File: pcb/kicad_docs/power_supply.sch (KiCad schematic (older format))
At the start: 22 parts, among them J10 ps_dc_htr_in_pcb, J7 ps_hv_dc_out_pcb, J8 ps_dc_htr_out_pcb, J9 ps_hv_ac_in_pcb

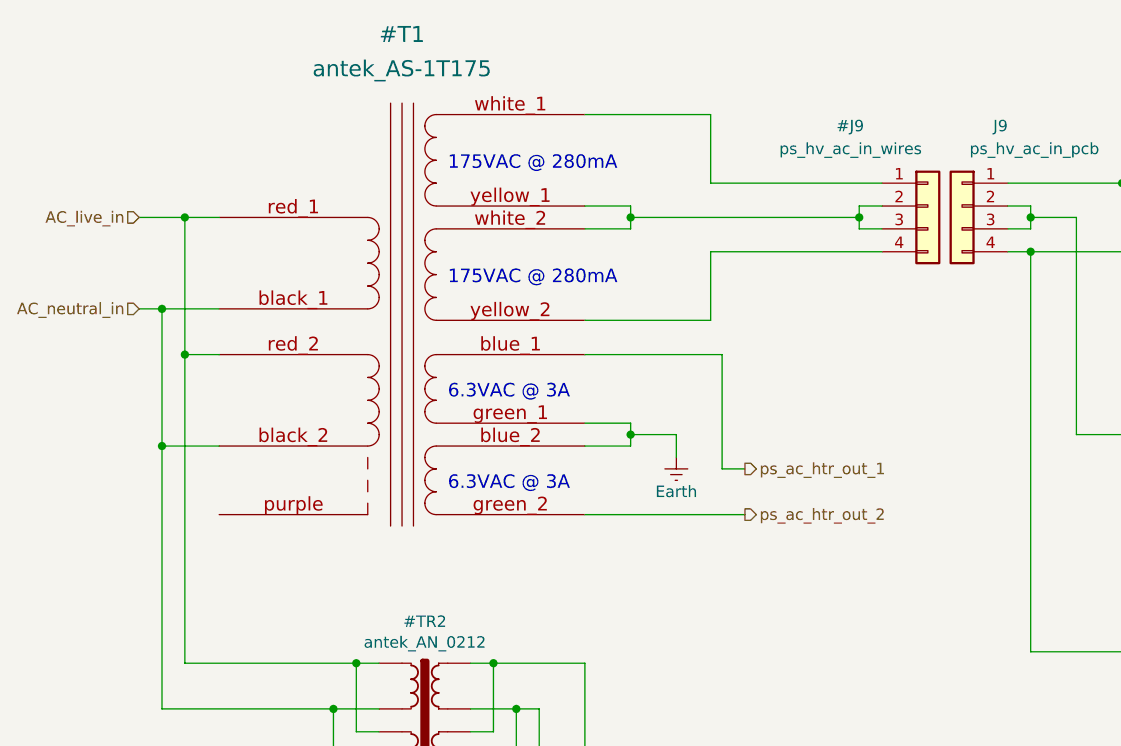
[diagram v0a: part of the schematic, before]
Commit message: add screen wire to power xformer
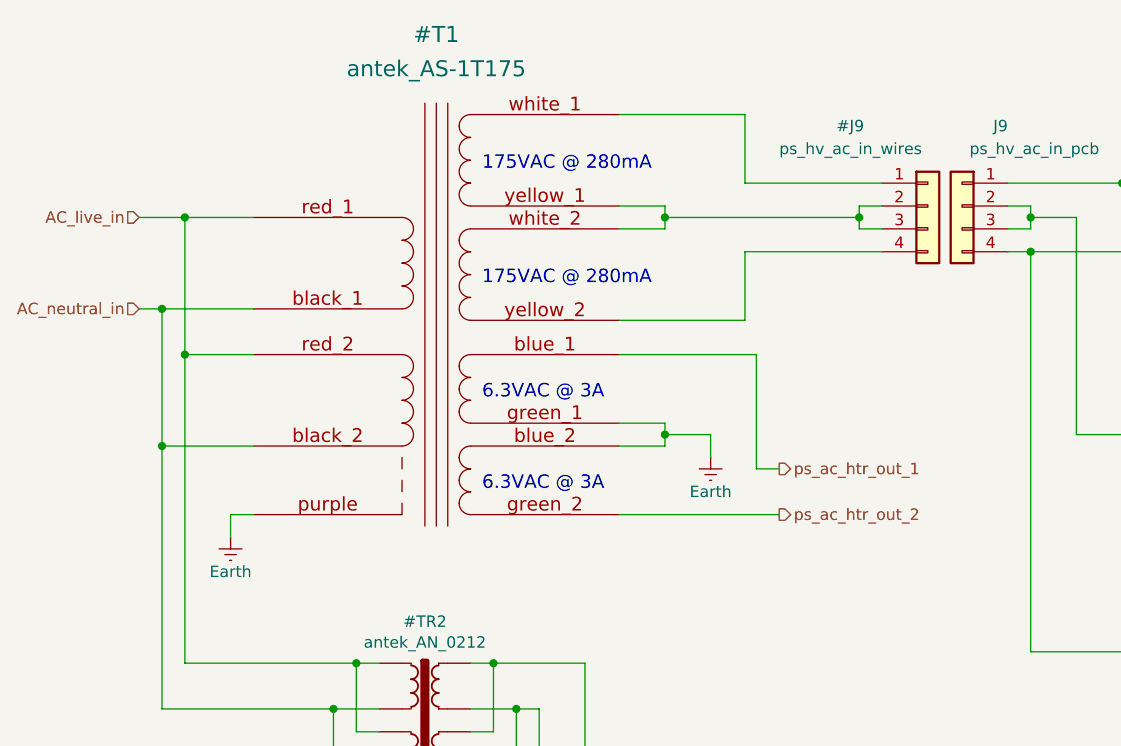
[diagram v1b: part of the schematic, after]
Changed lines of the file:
@@
 Sheet 4 4
 Title "It is the Champion"
-Date "2021-12-12"
+Date "2021-12-21"
 Rev "0.1"
 Comp ""
@@
 Text HLabel 1150 1750 0    50   Input ~ 0
 AC_live_in
-Text Notes 2500 2550 0    59   ~ 0
+Text Notes 2650 2550 0    59   ~ 0
 6.3VAC @ 3A
 Wire Wire Line
@@
 L custom_parts:antek_AS-1Txxx #T1
 U 1 1 61280AD8
-P 2300 2400
-F 0 "#T1" H 2300 3850 70  0000 C CNN
-F 1 "antek_AS-1T175" H 2300 3700 70  0000 C CNN
-F 2 "" H 2275 2475 60  0001 C CNN
-F 3 "" H 2275 2475 60  0000 C CNN
-	1    2300 2400
-	1    0    0    -1
-$EndComp
-Wire Wire Line
-	1500 2350 1350 2350
+P 2450 2400
+F 0 "#T1" H 2450 3850 70  0000 C CNN
+F 1 "antek_AS-1T175" H 2450 3700 70  0000 C CNN
+F 2 "" H 2425 2475 60  0001 C CNN
+F 3 "" H 2425 2475 60  0000 C CNN
+	1    2450 2400
+	1    0    0    -1
+$EndComp
+Wire Wire Line
+	1650 2350 1350 2350
 Wire Wire Line
 	1350 2350 1350 1750
 Wire Wire Line
-	1350 1750 1500 1750
-Wire Wire Line
-	1500 2750 1250 2750
+	1350 1750 1650 1750
+Wire Wire Line
+	1650 2750 1250 2750
 Wire Wire Line
 	1250 2750 1250 2150
 Wire Wire Line
-	1250 2150 1500 2150
+	1250 2150 1650 2150
 Connection ~ 1350 1750
 Connection ~ 1250 2150
 Wire Wire Line
-	3100 2650 3300 2650
+	3250 2650 3450 2650
 $Comp
 L Device:CP1 C17
@@
 Wire Wire Line
 	3650 5750 3650 5850
-Text Notes 2500 2950 0    59   ~ 0
+Text Notes 2650 2950 0    59   ~ 0
 6.3VAC @ 3A
 Wire Wire Line
-	3300 2750 3100 2750
+	3450 2750 3250 2750
 Wire Wire Line
 	3650 5150 3650 5050
@@
 $EndComp
 Wire Wire Line
-	3300 2750 3300 2700
-Wire Wire Line
-	3100 1800 3300 1800
-Wire Wire Line
-	3300 1800 3300 1750
-Wire Wire Line
-	3300 1700 3100 1700
-Text Notes 2500 1550 0    59   ~ 0
+	3450 2750 3450 2700
+Wire Wire Line
+	3250 1800 3450 1800
+Wire Wire Line
+	3450 1800 3450 1750
+Wire Wire Line
+	3450 1700 3250 1700
+Text Notes 2650 1550 0    59   ~ 0
 175VAC @ 280mA
 $Comp
@@
 L power:Earth #PWR?
 U 1 1 61F4E050
-P 3500 2800
+P 3650 2800
 AR Path="/61F4E050" Ref="#PWR?"  Part="1"
 AR Path="/61116F52/61F4E050" Ref="#PWR0103"  Part="1"
-F 0 "#PWR0103" H 3500 2550 50  0001 C CNN
-F 1 "Earth" H 3500 2650 50  0000 C CNN
-F 2 "" H 3500 2800 50  0001 C CNN
-F 3 "~" H 3500 2800 50  0001 C CNN
-	1    3500 2800
-	1    0    0    -1
-$EndComp
-Wire Wire Line
-	3500 2800 3500 2700
-Wire Wire Line
-	3500 2700 3300 2700
-Connection ~ 3300 2700
-Wire Wire Line
-	3300 2700 3300 2650
-Wire Wire Line
-	3800 2850 3700 2850
-Wire Wire Line
-	3700 2850 3700 2350
-Wire Wire Line
-	3100 2350 3700 2350
+F 0 "#PWR0103" H 3650 2550 50  0001 C CNN
+F 1 "Earth" H 3650 2650 50  0000 C CNN
+F 2 "" H 3650 2800 50  0001 C CNN
+F 3 "~" H 3650 2800 50  0001 C CNN
+	1    3650 2800
+	1    0    0    -1
+$EndComp
+Wire Wire Line
+	3650 2800 3650 2700
+Wire Wire Line
+	3650 2700 3450 2700
+Connection ~ 3450 2700
+Wire Wire Line
+	3450 2700 3450 2650
+Wire Wire Line
+	3950 2850 3850 2850
+Wire Wire Line
+	3850 2850 3850 2350
+Wire Wire Line
+	3250 2350 3850 2350
 Wire Wire Line
 	4300 1700 4300 1750
@@
 	4300 1700 4400 1700
 Wire Wire Line
-	4300 1750 3300 1750
+	4300 1750 3450 1750
 Connection ~ 4300 1750
 Wire Wire Line
 	4300 1750 4300 1800
 Wire Wire Line
-	4400 1600 3650 1600
-Wire Wire Line
-	3650 1600 3650 1300
-Wire Wire Line
-	3650 1300 3100 1300
-Wire Wire Line
-	3100 2200 3650 2200
-Wire Wire Line
-	3650 2200 3650 1900
-Wire Wire Line
-	3650 1900 4400 1900
+	4400 1600 3800 1600
+Wire Wire Line
+	3800 1600 3800 1300
+Wire Wire Line
+	3800 1300 3250 1300
+Wire Wire Line
+	3250 2200 3800 2200
+Wire Wire Line
+	3800 2200 3800 1900
+Wire Wire Line
+	3800 1900 4400 1900
 $Comp
 L Diode:1N4007 D4
@@
 Wire Wire Line
 	6050 1600 6150 1600
-Connection ~ 3300 1750
-Wire Wire Line
-	3300 1750 3300 1700
+Connection ~ 3450 1750
+Wire Wire Line
+	3450 1750 3450 1700
 Wire Wire Line
 	6950 3650 7250 3650
@@
 Wire Wire Line
 	5050 1750 5050 1800
-Text Notes 2500 2050 0    59   ~ 0
+Text Notes 2650 2050 0    59   ~ 0
 175VAC @ 280mA
 $Comp
@@
 	4800 6650 5400 6650
 Wire Wire Line
-	3100 3050 3800 3050
+	3250 3050 3950 3050
 Text Notes 3400 7050 0    50   ~ 0
 DC heater supply is referenced\nto the chassis through one of\nthe metal standoffs.
@@
 Text Notes 7950 2700 0    50   ~ 0
 240VDC
-Text HLabel 3800 3050 2    50   Output ~ 0
+Text HLabel 3950 3050 2    50   Output ~ 0
 ps_ac_htr_out_2
-Text HLabel 3800 2850 2    50   Output ~ 0
+Text HLabel 3950 2850 2    50   Output ~ 0
 ps_ac_htr_out_1
 Text HLabel 7050 6100 2    50   Output ~ 0
@@
 Text Notes 4950 5450 0    50   ~ 0
 12.6VDC
+$Comp
+L power:Earth #PWR?
+U 1 1 61C4BC57
+P 1550 3150
+AR Path="/61C4BC57" Ref="#PWR?"  Part="1"
+AR Path="/61116F52/61C4BC57" Ref="#PWR?"  Part="1"
+F 0 "#PWR?" H 1550 2900 50  0001 C CNN
+F 1 "Earth" H 1550 3000 50  0000 C CNN
+F 2 "" H 1550 3150 50  0001 C CNN
+F 3 "~" H 1550 3150 50  0001 C CNN
+	1    1550 3150
+	1    0    0    -1
+$EndComp
+Wire Wire Line
+	1550 3150 1550 3050
+Wire Wire Line
+	1550 3050 1650 3050
 $EndSCHEMATC
